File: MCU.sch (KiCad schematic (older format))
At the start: 10 parts

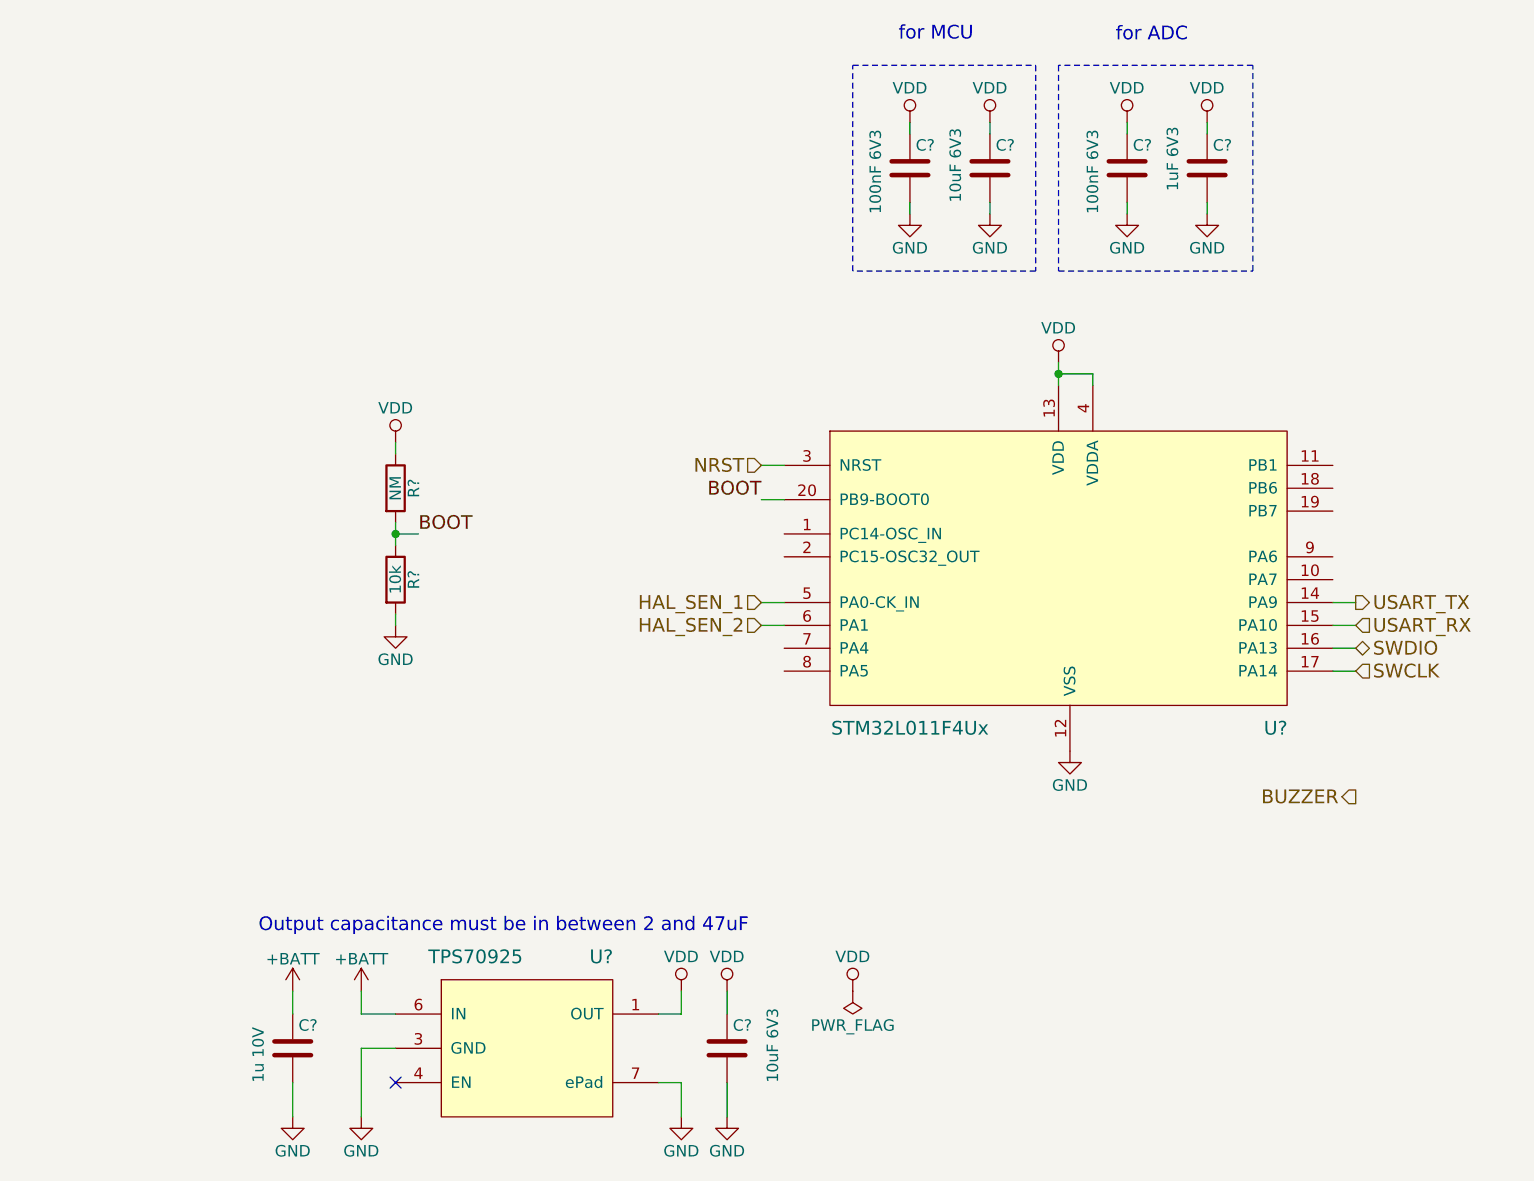
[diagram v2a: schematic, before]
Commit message: Added Boost converter
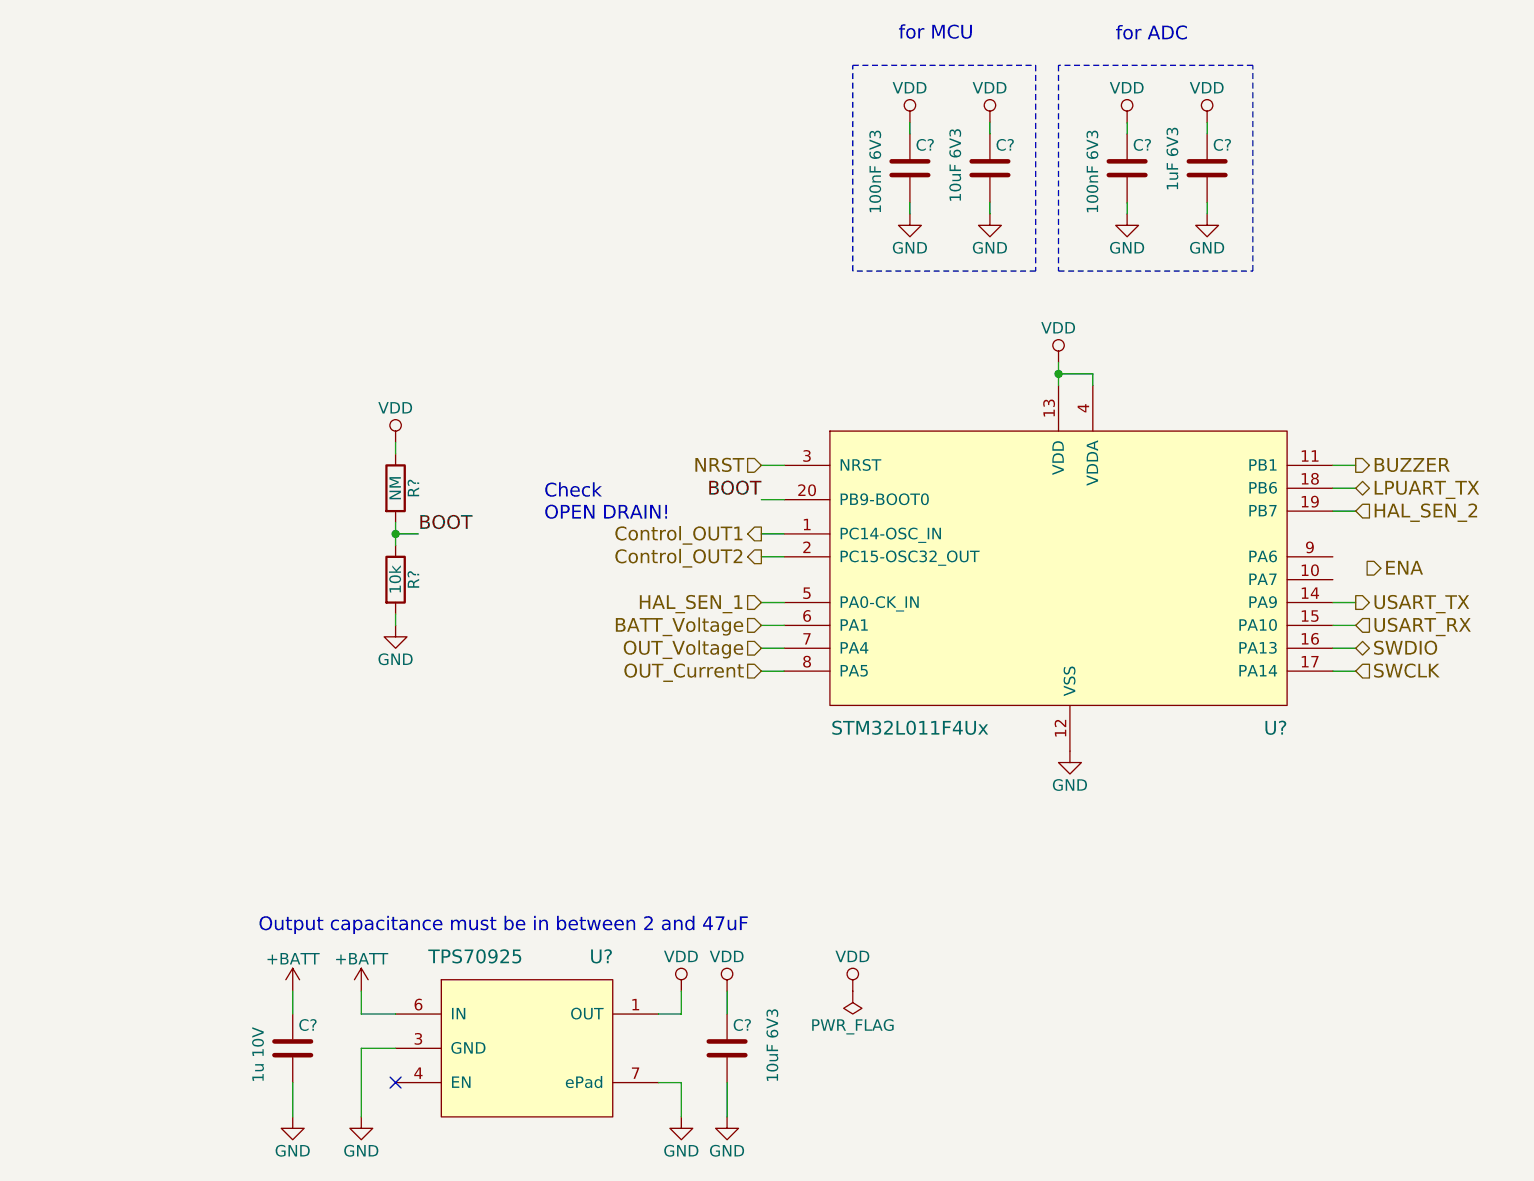
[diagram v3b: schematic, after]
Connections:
- net BUZZER: now also U?.11 (PB1)
- net HAL_SEN_2: now also U?.19 (PB7); no longer U?.6 (PA1)
- net Control_OUT1: now reaches U?.1 (PC14-OSC_IN)
- net LPUART_TX: now reaches U?.18 (PB6)
- net Control_OUT2: now reaches U?.2 (PC15-OSC32_OUT)
- net OUT_Voltage: now reaches U?.7 (PA4)
- net OUT_Current: now reaches U?.8 (PA5)
- new net BATT_Voltage: U?.6 (PA1)
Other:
- note added: "Check\nOPEN DRAIN!\n"
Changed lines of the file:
@@
 $Descr A4 11693 8268
 encoding utf-8
-Sheet 2 2
+Sheet 2 4
 Title ""
 Date ""
@@
 $EndComp
 Wire Wire Line
-	6100 3250 6100 3350
+	6100 3250 6100 3300
+Wire Wire Line
+	6100 3300 6100 3350
 Wire Wire Line
 	6250 3350 6250 3300
@@
 $EndComp
 Wire Wire Line
-	3200 3950 3200 4050
+	3200 3950 3200 4000
+Wire Wire Line
+	3200 4000 3200 4050
 Wire Wire Line
 	3200 3650 3200 3600
@@
 Wire Wire Line
 	4800 4300 4900 4300
-Text HLabel 4800 4400 0    60   Input ~ 0
+Text HLabel 7400 3900 2    60   Input ~ 0
 HAL_SEN_2
-Wire Wire Line
-	4800 4400 4900 4400
 $Comp
 L PWR_FLAG #FLG?
@@
 	1    0    0    -1
 $EndComp
-Text HLabel 7400 5150 0    60   Output ~ 0
+Text HLabel 7400 3700 2    60   Output ~ 0
 BUZZER
+Text HLabel 4800 4000 0    60   Output ~ 0
+Control_OUT1
+Text HLabel 4800 4100 0    60   Output ~ 0
+Control_OUT2
+Text HLabel 7450 4150 2    60   Output ~ 0
+ENA
+Text HLabel 4800 4500 0    60   Input ~ 0
+OUT_Voltage
+Text HLabel 4800 4600 0    60   Input ~ 0
+OUT_Current
+Wire Wire Line
+	4800 4400 4900 4400
+Wire Wire Line
+	4800 4500 4900 4500
+Wire Wire Line
+	4800 4600 4900 4600
+Text HLabel 4800 4400 0    60   Input ~ 0
+BATT_Voltage
+Text HLabel 7400 3800 2    60   BiDi ~ 0
+LPUART_TX
+Wire Wire Line
+	7300 3800 7400 3800
+Wire Wire Line
+	7300 3700 7400 3700
+Wire Wire Line
+	7300 3900 7400 3900
+Wire Wire Line
+	4800 4000 4900 4000
+Wire Wire Line
+	4800 4100 4900 4100
+Text Notes 3850 3950 0    60   ~ 0
+Check\nOPEN DRAIN!\n
 $EndSCHEMATC

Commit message: Added Input for coil and battery
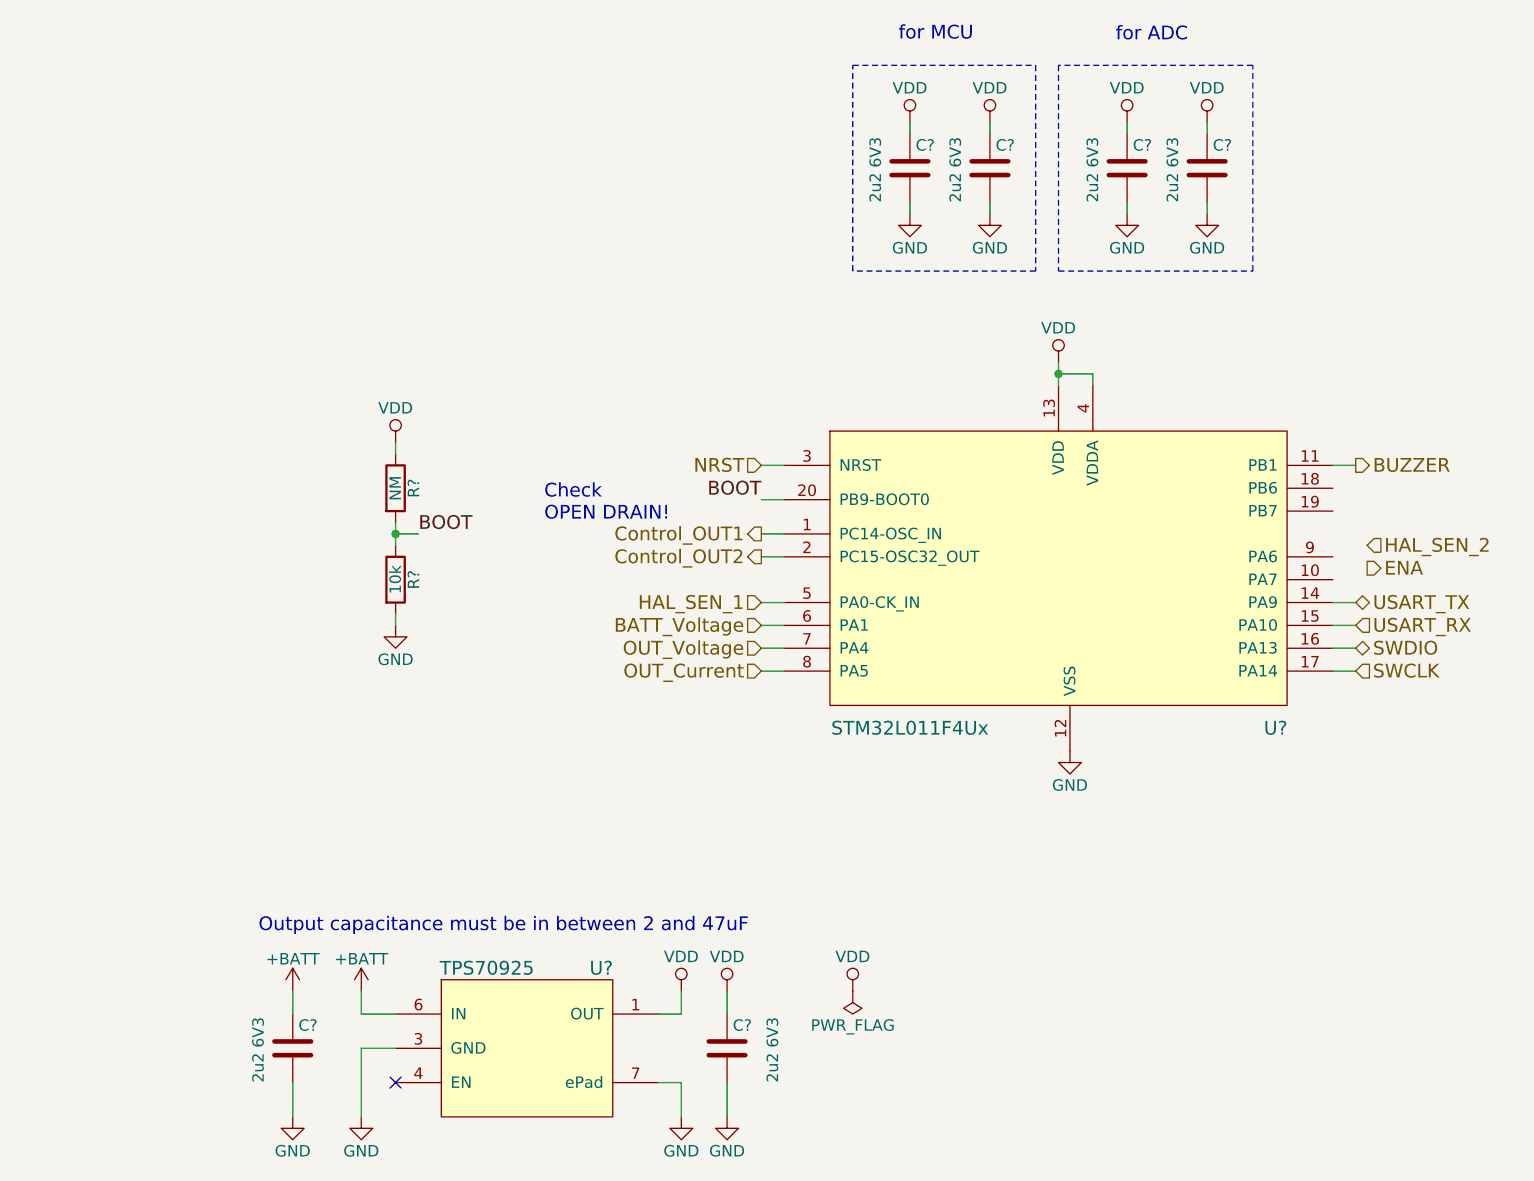
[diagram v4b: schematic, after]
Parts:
- removed U?: STM32L011F4Ux, Housings_DFN_QFN:ST_UFQFPN-20_3x3mm_Pitch0.5mm, symbol STM32L011F4Ux
- removed U?: TPS70925, lakotamm-miscellaneous:WSON-6_2x2mm_Pitch0.65mm, symbol TPS709
- added U?: STM32L011F4Ux, Housings_DFN_QFN:ST_UFQFPN-20_3x3mm_Pitch0.5mm, symbol STM32L011F4Ux
- added U?: TPS70925, lakotamm-miscellaneous:WSON-6_2x2mm_Pitch0.65mm, symbol TPS709
- C? (x2): value 10uF 6V3 -> 2u2 6V3
- C?: value 1u 10V -> 2u2 6V3
- C? (x2): value 100nF 6V3 -> 2u2 6V3
- C?: value 1uF 6V3 -> 2u2 6V3
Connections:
- net +BATT: now also U?.6 (IN)
- net BATT_Voltage: now also U?.6 (PA1)
- net BOOT: now also U?.20 (PB9-BOOT0)
- net BUZZER: now also U?.11 (PB1)
- net Control_OUT1: now also U?.1 (PC14-OSC_IN)
- net Control_OUT2: now also U?.2 (PC15-OSC32_OUT)
- net GND: now also U?.12 (VSS), U?.3 (GND), U?.7 (ePad)
- net HAL_SEN_1: now also U?.5 (PA0-CK_IN)
- net NRST: now also U?.3 (NRST)
- net OUT_Current: now also U?.8 (PA5)
- net OUT_Voltage: now also U?.7 (PA4)
- net SWCLK: now also U?.17 (PA14)
- net SWDIO: now also U?.16 (PA13)
- net USART_RX: now also U?.15 (PA10)
- net USART_TX: now also U?.14 (PA9)
- net VDD: now also U?.1 (OUT), U?.13 (VDD), U?.4 (VDDA)
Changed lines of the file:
@@
 $EndDescr
-$Comp
-L STM32L011F4Ux U?
-U 1 1 5A9B30A2
-P 6150 4200
-F 0 "U?" H 7050 3550 60  0000 C CNN
-F 1 "STM32L011F4Ux" H 5450 3550 60  0000 C CNN
-F 2 "Housings_DFN_QFN:ST_UFQFPN-20_3x3mm_Pitch0.5mm" H 6150 3300 60  0001 C CNN
-F 3 "http://www.st.com/resource/en/datasheet/stm32l011f4.pdf" H 6150 3150 60  0001 C CNN
-	1    6150 4200
-	1    0    0    -1
-$EndComp
 $Comp
 L VDD #PWR?
@@
 $EndComp
 Wire Wire Line
-	6100 3250 6100 3300
-Wire Wire Line
-	6100 3300 6100 3350
+	6100 3250 6100 3350
 Wire Wire Line
 	6250 3350 6250 3300
@@
 F 3 "" H 6150 4950 50  0001 C CNN
 	1    6150 4950
-	1    0    0    -1
-$EndComp
-$Comp
-L TPS709 U?
-U 1 1 5A9B30C7
-P 3800 6250
-F 0 "U?" H 4100 6650 60  0000 C CNN
-F 1 "TPS70925" H 3550 6650 60  0000 C CNN
-F 2 "lakotamm-miscellaneous:WSON-6_2x2mm_Pitch0.65mm" H 3850 5600 60  0001 C CNN
-F 3 "http://www.ti.com/lit/ds/symlink/tps709.pdf" H 3800 5750 60  0001 C CNN
-	1    3800 6250
 	1    0    0    -1
 $EndComp
@@
 P 4650 6250
 F 0 "C?" H 4675 6350 50  0000 L CNN
-F 1 "10uF 6V3" V 4850 6100 50  0000 L CNN
+F 1 "2u2 6V3" V 4850 6100 50  0000 L CNN
 F 2 "" H 4688 6100 50  0001 C CNN
 F 3 "" H 4650 6250 50  0001 C CNN
@@
 P 2750 6250
 F 0 "C?" H 2775 6350 50  0000 L CNN
-F 1 "1u 10V" V 2600 6100 50  0000 L CNN
+F 1 "2u2 6V3" V 2600 6100 50  0000 L CNN
 F 2 "" H 2788 6100 50  0001 C CNN
 F 3 "" H 2750 6250 50  0001 C CNN
@@
 P 5450 2400
 F 0 "C?" H 5475 2500 50  0000 L CNN
-F 1 "100nF 6V3" V 5300 2200 50  0000 L CNN
+F 1 "2u2 6V3" V 5300 2250 50  0000 L CNN
 F 2 "" H 5488 2250 50  0001 C CNN
 F 3 "" H 5450 2400 50  0001 C CNN
@@
 P 5800 2400
 F 0 "C?" H 5825 2500 50  0000 L CNN
-F 1 "10uF 6V3" V 5650 2250 50  0000 L CNN
+F 1 "2u2 6V3" V 5650 2250 50  0000 L CNN
 F 2 "" H 5838 2250 50  0001 C CNN
 F 3 "" H 5800 2400 50  0001 C CNN
@@
 P 6400 2400
 F 0 "C?" H 6425 2500 50  0000 L CNN
-F 1 "100nF 6V3" V 6250 2200 50  0000 L CNN
+F 1 "2u2 6V3" V 6250 2250 50  0000 L CNN
 F 2 "" H 6438 2250 50  0001 C CNN
 F 3 "" H 6400 2400 50  0001 C CNN
@@
 P 6750 2400
 F 0 "C?" H 6775 2500 50  0000 L CNN
-F 1 "1uF 6V3" V 6600 2300 50  0000 L CNN
+F 1 "2u2 6V3" V 6600 2250 50  0000 L CNN
 F 2 "" H 6788 2250 50  0001 C CNN
 F 3 "" H 6750 2400 50  0001 C CNN
@@
 $EndComp
 Wire Wire Line
-	3200 3950 3200 4000
-Wire Wire Line
-	3200 4000 3200 4050
+	3200 3950 3200 4050
 Wire Wire Line
 	3200 3650 3200 3600
@@
 Wire Wire Line
 	4800 3850 4900 3850
-Text HLabel 7400 4300 2    60   Output ~ 0
+Text HLabel 7400 4300 2    60   BiDi ~ 0
 USART_TX
 Text HLabel 7400 4400 2    60   Input ~ 0
@@
 Wire Wire Line
 	4800 4300 4900 4300
-Text HLabel 7400 3900 2    60   Input ~ 0
+Text HLabel 7450 4050 2    60   Input ~ 0
 HAL_SEN_2
 $Comp
@@
 Text HLabel 4800 4400 0    60   Input ~ 0
 BATT_Voltage
-Text HLabel 7400 3800 2    60   BiDi ~ 0
-LPUART_TX
-Wire Wire Line
-	7300 3800 7400 3800
 Wire Wire Line
 	7300 3700 7400 3700
-Wire Wire Line
-	7300 3900 7400 3900
 Wire Wire Line
 	4800 4000 4900 4000
@@
 Text Notes 3850 3950 0    60   ~ 0
 Check\nOPEN DRAIN!\n
+$Comp
+L STM32L011F4Ux U?
+U 1 1 5AA7A3A1
+P 6150 4200
+F 0 "U?" H 7050 3550 60  0000 C CNN
+F 1 "STM32L011F4Ux" H 5450 3550 60  0000 C CNN
+F 2 "Housings_DFN_QFN:ST_UFQFPN-20_3x3mm_Pitch0.5mm" H 6150 3300 60  0001 C CNN
+F 3 "http://www.st.com/resource/en/datasheet/stm32l011f4.pdf" H 6150 3150 60  0001 C CNN
+F 4 "STM32L011F4U6TR" H 6150 5150 60  0001 C CNN "MPN"
+	1    6150 4200
+	1    0    0    -1
+$EndComp
+$Comp
+L TPS709 U?
+U 1 1 5AA7A66F
+P 3800 6250
+F 0 "U?" H 4100 6600 60  0000 C CNN
+F 1 "TPS70925" H 3600 6600 60  0000 C CNN
+F 2 "lakotamm-miscellaneous:WSON-6_2x2mm_Pitch0.65mm" H 3850 5600 60  0001 C CNN
+F 3 "http://www.ti.com/lit/ds/symlink/tps709.pdf" H 3800 5750 60  0001 C CNN
+F 4 "TPS70925DBV" H 3800 6600 60  0001 C CNN "MPN"
+	1    3800 6250
+	1    0    0    -1
+$EndComp
 $EndSCHEMATC

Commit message: Started working on the charger
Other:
- note added: "All decoupling capacitors have purposely the same value\n"
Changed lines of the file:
@@
 LIBS:contrib
 LIBS:valves
-LIBS:stm32
 LIBS:lakotamm-microprocessors
 LIBS:lakotamm-powersupply
 LIBS:lakotamm-sensor
 LIBS:lakotamm-transistor
+LIBS:lakotamm-wireless
 LIBS:F3K_Battery_manager-cache
 EELAYER 25 0
@@
 	1    0    0    -1
 $EndComp
+Text Notes 4950 3000 0    60   ~ 0
+All decoupling capacitors have purposely the same value\n
 $EndSCHEMATC

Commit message: small updates
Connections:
- net labels added: Control_OUT
- net labels removed: Control_OUT1, Control_OUT2
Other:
- note removed: "Check\nOPEN DRAIN!\n"
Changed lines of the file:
@@
 LIBS:power
 LIBS:device
-LIBS:switches
-LIBS:relays
-LIBS:motors
-LIBS:transistors
-LIBS:conn
 LIBS:linear
 LIBS:regul
-LIBS:74xx
-LIBS:cmos4000
 LIBS:adc-dac
 LIBS:memory
@@
 LIBS:digital-audio
 LIBS:philips
-LIBS:display
 LIBS:cypress
 LIBS:siliconi
@@
 LIBS:atmel
 LIBS:contrib
-LIBS:valves
 LIBS:lakotamm-microprocessors
 LIBS:lakotamm-powersupply
@@
 LIBS:lakotamm-transistor
 LIBS:lakotamm-wireless
+LIBS:MCU_ST_STM32
+LIBS:Transistor
+LIBS:Connector
 LIBS:F3K_Battery_manager-cache
 EELAYER 25 0
@@
 Wire Wire Line
 	4800 4300 4900 4300
-Text HLabel 7450 4050 2    60   Input ~ 0
+Text HLabel 8050 5250 0    60   Input ~ 0
 HAL_SEN_2
 $Comp
@@
 Text HLabel 7400 3700 2    60   Output ~ 0
 BUZZER
-Text HLabel 4800 4000 0    60   Output ~ 0
-Control_OUT1
-Text HLabel 4800 4100 0    60   Output ~ 0
-Control_OUT2
-Text HLabel 7450 4150 2    60   Output ~ 0
+Text HLabel 8050 5550 0    60   Output ~ 0
+Control_OUT
+Text HLabel 8050 5400 0    60   Output ~ 0
 ENA
 Text HLabel 4800 4500 0    60   Input ~ 0
@@
 Wire Wire Line
 	4800 4100 4900 4100
-Text Notes 3850 3950 0    60   ~ 0
-Check\nOPEN DRAIN!\n
 $Comp
 L STM32L011F4Ux U?
